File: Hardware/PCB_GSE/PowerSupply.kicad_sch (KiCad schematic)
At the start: 67 parts, among them J2 Vin_XT30PW-F, U2 MPQ9843GLE-5-AEC1-Z, U3 MP28167GQ-B-P, U4 TLV75733PDBVR

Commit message: fix : done silkscreen and finition
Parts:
- renumbered C44 to C21, C42 to C30, C32 to C31, C36 to C33, C24 to C34, C19 to C35, C43 to C36, C33 to C37, C16 to C38, C41 to C39, C22 to C40, C13 to C41, C34 to C42, C12 to C43, C26 to C44, C18 to C45, C21 to C46, C14 to C47, C29 to C48, C31 to C49, C15 to C50, C25 to C51, C23 to C52, C20 to C53, C17 to C54, C39 to C55, C38 to C56, C37 to C57, C35 to C58, C28 to C59, C40 to C60, C27 to C61, C30 to C62, LED4 to D6, LED2 to D7, LED3 to D8, FB2 to FB4, J2 to J8, L2 to L1, L1 to L2, R33 to R18, R31 to R20, R34 to R26, R35 to R27, R26 to R28, R30 to R31, R22 to R33, R17 to R34, R18 to R35, R29 to R36, R20 to R37, R15 to R38, R14 to R39, R27 to R40, R28 to R41, R19 to R42, R16 to R43, R21 to R44, R23 to R45, R25 to R46, R24 to R47, U3 to U10, U2 to U8, U4 to U9

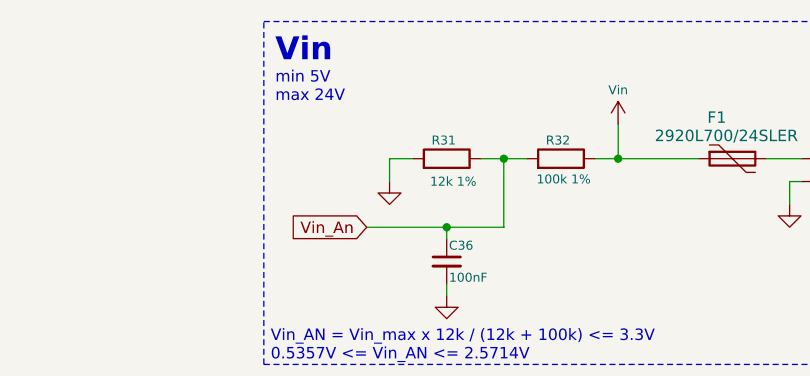
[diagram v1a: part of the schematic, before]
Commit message: fix(gse): Vin servo
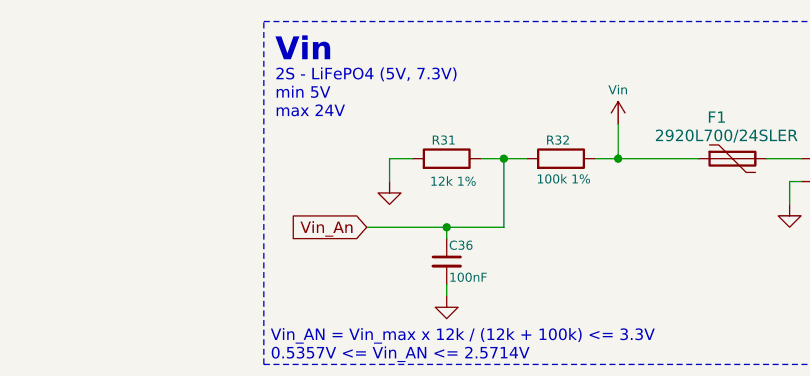
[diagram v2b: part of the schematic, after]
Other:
- note added: "2S - LiFePO4 (5V, 7.3V) min 5V max 24V"
- note removed: "min 5V max 24V"
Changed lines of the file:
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@@
 		)
 	)
-	(text "min 5V\nmax 24V"
+	(text "2S - LiFePO4 (5V, 7.3V)\nmin 5V\nmax 24V"
 		(exclude_from_sim no)
-		(at 208.28 18.288 0)
+		(at 208.28 18.034 0)
 		(effects
 			(font

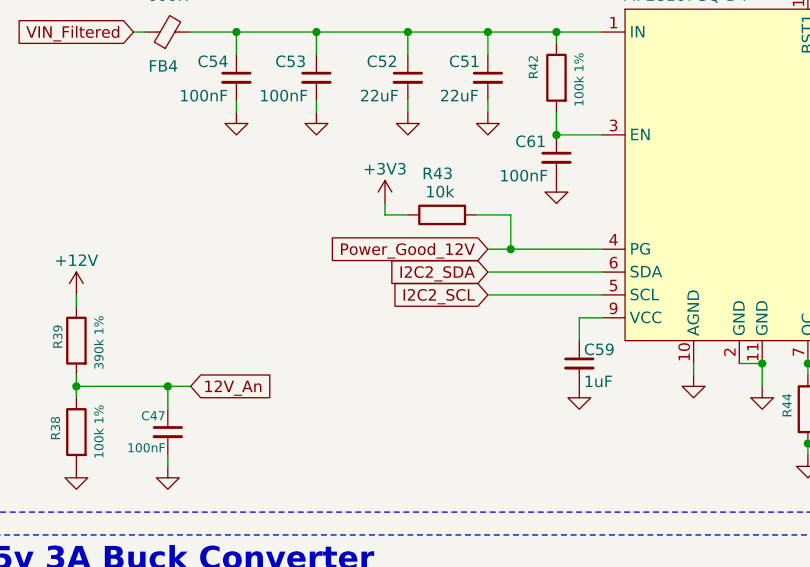
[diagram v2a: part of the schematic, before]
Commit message: fix(gse): change Servo3_PWM -> TIM1_CH2, change Valve1/2_Open pin
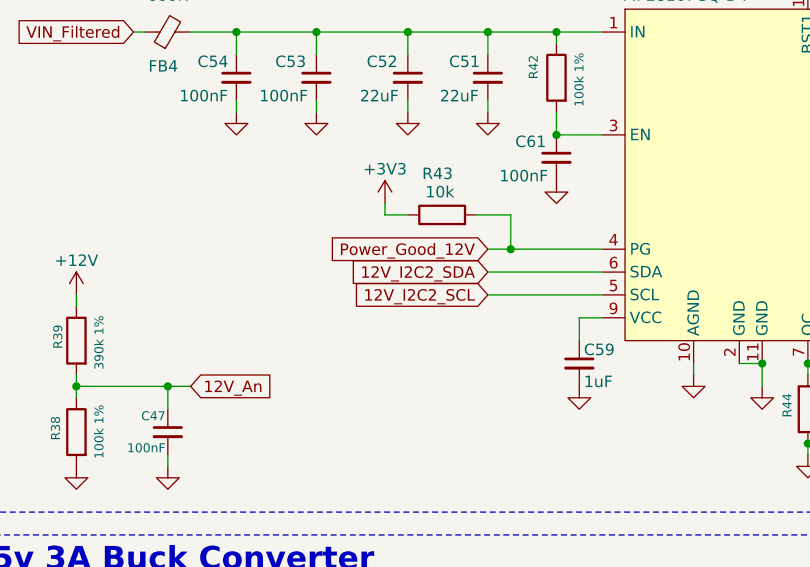
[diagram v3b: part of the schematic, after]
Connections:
- net I2C2_SCL renamed 12V_I2C2_SCL
- net I2C2_SDA renamed 12V_I2C2_SDA
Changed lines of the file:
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@@
 		)
 	)
-	(global_label "I2C2_SDA"
+	(global_label "12V_I2C2_SDA"
 		(shape input)
 		(at 69.85 96.52 180)
@@
 		)
 		(property "Intersheetrefs" "${INTERSHEET_REFS}"
-			(at 58.0353 96.52 0)
+			(at 53.5601 96.52 0)
 			(effects
 				(font
@@
 		)
 	)
-	(global_label "I2C2_SCL"
+	(global_label "12V_I2C2_SCL"
 		(shape input)
 		(at 69.85 99.06 180)
@@
 		)
 		(property "Intersheetrefs" "${INTERSHEET_REFS}"
-			(at 58.0958 99.06 0)
+			(at 53.6206 99.06 0)
 			(effects
 				(font

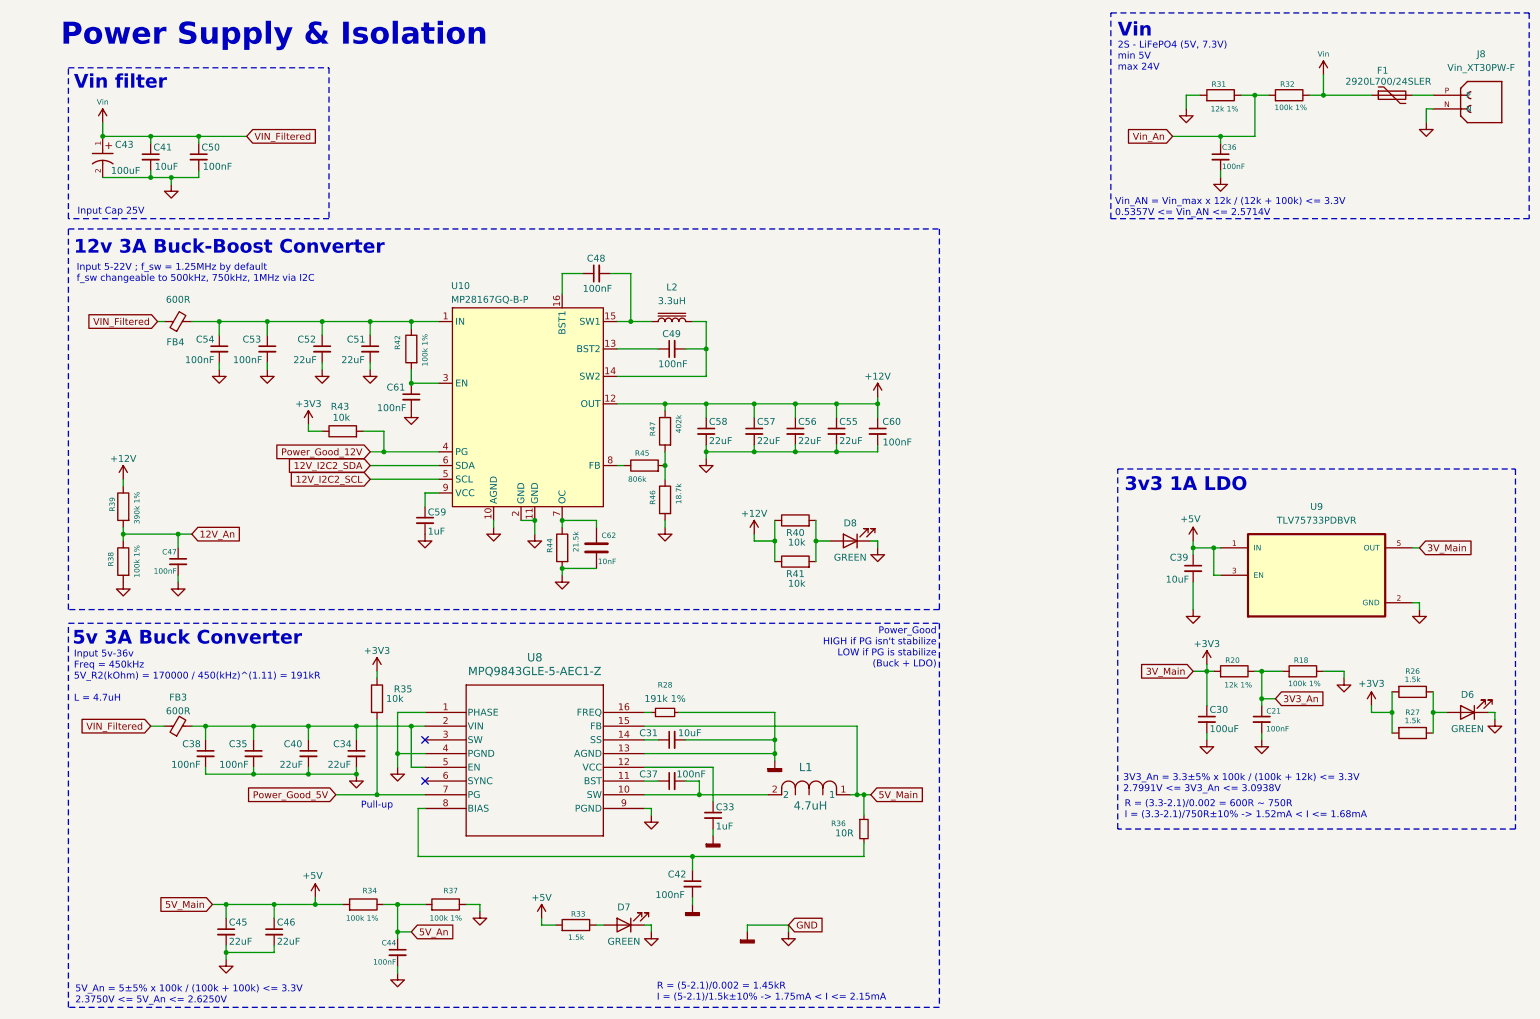
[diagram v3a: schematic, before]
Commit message: fix: silkscreen green<->black + fix silkscreen + connect shield to gnd  in pressure sensor + fix/add doc
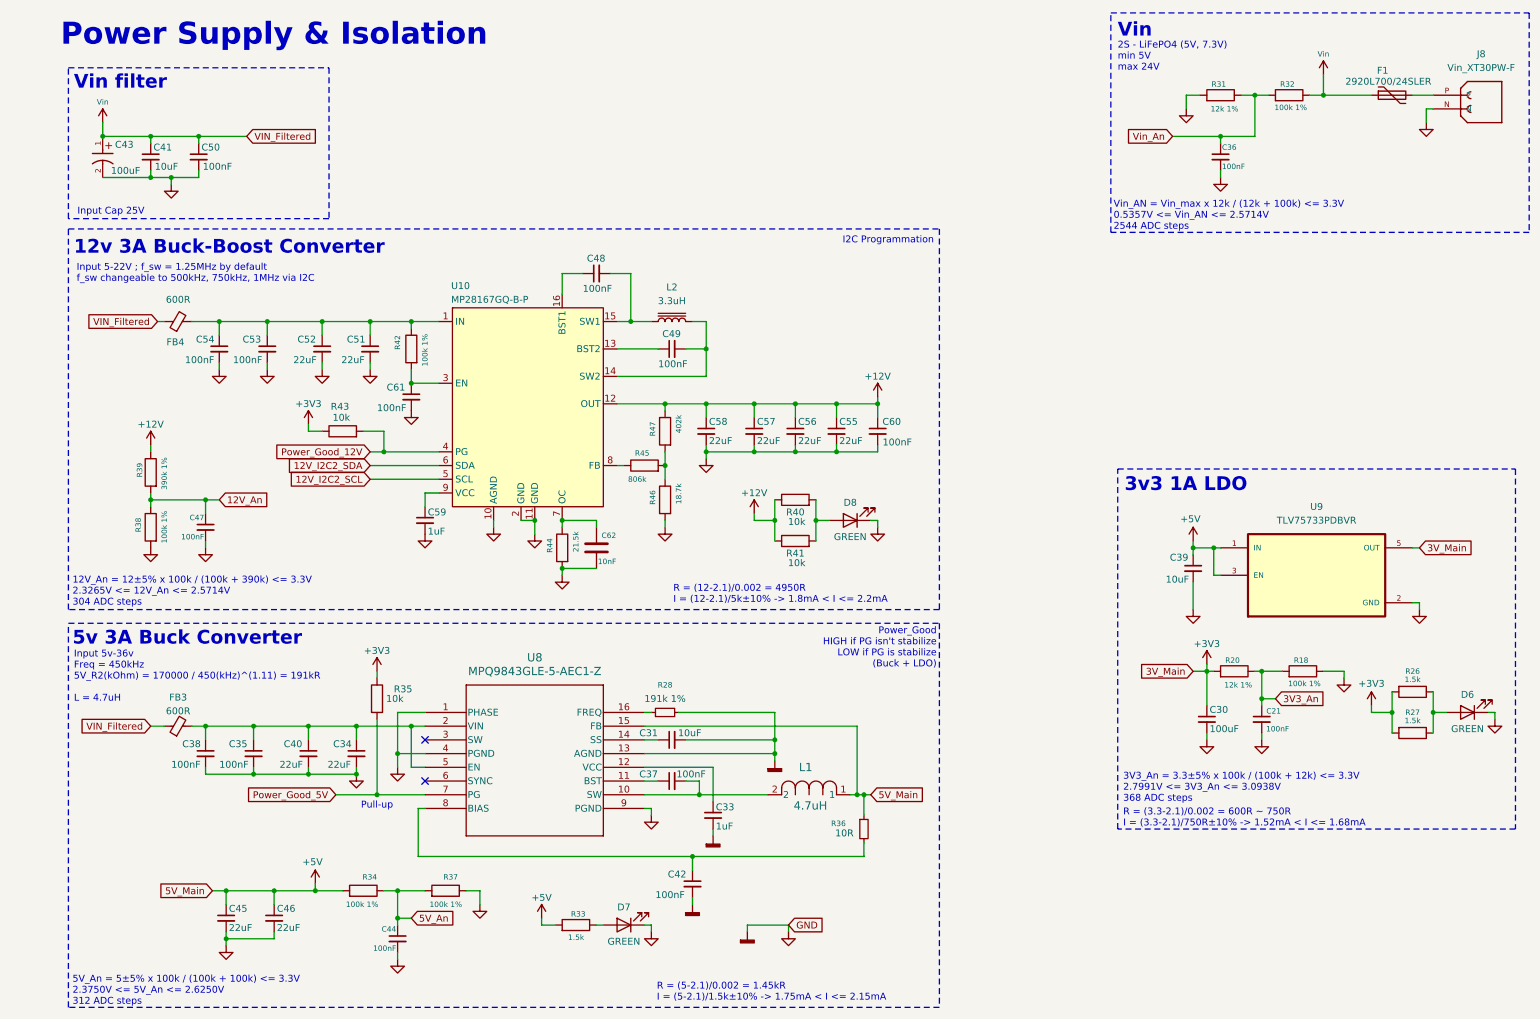
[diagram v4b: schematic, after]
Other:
- note added: "12V_An = 12±5% x 100k / (100k + 390k) <= 3.3V 2.3265V <= 12V_An <= 2.5714V 304 ADC steps"
- note added: "3V3_An = 3.3±5% x 100k / (100k + 12k) <= 3.3V 2.7991V <= 3V3_An <= 3.0938V 368 ADC steps"
- note added: "5V_An = 5±5% x 100k / (100k + 100k) <= 3.3V 2.3750V <= 5V_An <= 2.6250V 312 ADC steps"
- note added: "I2C Programmation"
- note added: "R = (12-2.1)/0.002 = 4950R I = (12-2.1)/5k±10% -> 1.8mA < I <= 2.2mA"
- note added: "Vin_AN = Vin_max x 12k / (12k + 100k) <= 3.3V 0.5357V <= Vin_AN <= 2.5714V 2544 ADC steps"
- note removed: "3V3_An = 3.3±5% x 100k / (100k + 12k) <= 3.3V 2.7991V <= 3V3_An <= 3.0938V"
- note removed: "5V_An = 5±5% x 100k / (100k + 100k) <= 3.3V 2.3750V <= 5V_An <= 2.6250V"
- note removed: "Vin_AN = Vin_max x 12k / (12k + 100k) <= 3.3V 0.5357V <= Vin_AN <= 2.5714V"
- moved on the sheet: C44, C45, C46, C47, D8, R34, R37, R38, R39, R40, R41

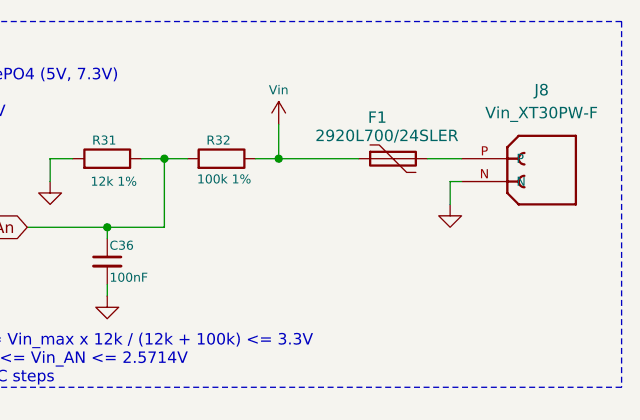
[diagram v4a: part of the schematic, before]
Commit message: fix : add polyfuses and fix 90 deg servo connectors
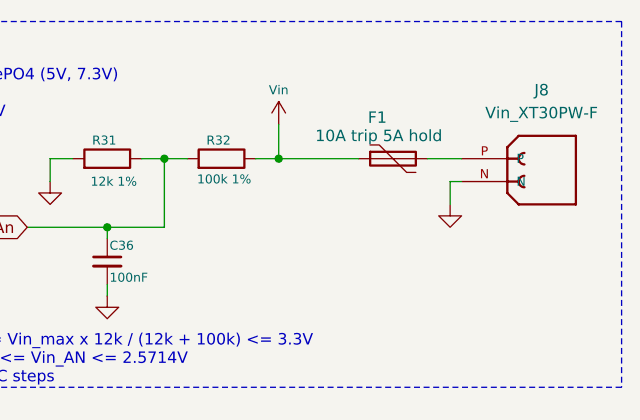
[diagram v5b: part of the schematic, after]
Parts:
- F1: value 2920L700/24SLER -> 10A trip 5A hold; DigiKey_Part_Number 18-2920L700/24SLERCT-ND -> 18-2920L500/24SLDRCT-ND; Manufacturer_Part_Number 2920L700/24SLER -> 2920L500/24SLDR
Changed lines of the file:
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@@
 			)
 		)
-		(property "Value" "2920L700/24SLER"
+		(property "Value" "10A trip 5A hold"
 			(at 250.444 25.4 90)
 			(effects
@@
 			)
 		)
-		(property "Datasheet" "https://www.digikey.ca/en/products/detail/littelfuse-inc/2920L700-24SLER/12807015"
+		(property "Datasheet" "https://www.digikey.ca/en/products/detail/littelfuse-inc/2920L500-24SLDR/12807024"
 			(at 259.08 27.94 0)
 			(effects
@@
 			)
 		)
-		(property "DigiKey_Part_Number" "18-2920L700/24SLERCT-ND"
+		(property "DigiKey_Part_Number" "18-2920L500/24SLDRCT-ND"
 			(at 259.08 27.94 90)
 			(effects
@@
 			)
 		)
-		(property "Manufacturer_Part_Number" "2920L700/24SLER"
+		(property "Manufacturer_Part_Number" "2920L500/24SLDR"
 			(at 259.08 27.94 90)
 			(effects

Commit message: feature : Done v1 and send to fab
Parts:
- C33, C59: DigiKey_Part_Number 399-C0603C105K4RACTUCT-ND -> 1276-1029-1-ND; Manufacturer_Part_Number C0603C105K4RACTU -> CL21B105KBFNNNE
- J8: Manufacturer_Part_Number (none) -> -
- R26, R27, R33: DigiKey_Part_Number P1.5KDBCT-ND -> 311-1.50KCRCT-ND; Manufacturer_Part_Number ERA-3AEB152V -> RC0805FR-071K5L
- R28: DigiKey_Part_Number P191KDBCT-ND -> 311-191KCRCT-ND; Manufacturer_Part_Number ERA-3AEB1913V -> RC0805FR-07191KL
- R35, R40, R41, R43: DigiKey_Part_Number 311-10.0KHRCT-ND -> 541-10.0KCCT-ND; Manufacturer_Part_Number RC0603FR-0710KL -> CRCW080510K0FKEA
- R36: DigiKey_Part_Number 541-10.0LCT-ND -> 311-10.0CRCT-ND; Manufacturer_Part_Number CRCW040210R0FKED -> RC0805FR-0710RL
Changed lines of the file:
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@@
 			)
 		)
-		(property "Datasheet" "https://www.digikey.ca/en/products/detail/panasonic-electronic-components/ERA-3AEB152V/1465858"
+		(property "Datasheet" "https://www.digikey.ca/en/products/detail/yageo/RC0805FR-071K5L/727496"
 			(at 107.95 181.61 0)
 			(effects
@@
 			)
 		)
-		(property "DigiKey_Part_Number" "P1.5KDBCT-ND"
+		(property "DigiKey_Part_Number" "311-1.50KCRCT-ND"
 			(at 107.95 181.61 90)
 			(effects
@@
 			)
 		)
-		(property "Manufacturer_Part_Number" "ERA-3AEB152V"
+		(property "Manufacturer_Part_Number" "RC0805FR-071K5L"
 			(at 107.95 181.61 90)
 			(effects
@@
 			)
 		)
-		(property "Datasheet" ""
+		(property "Datasheet" "-"
 			(at 271.78 27.94 0)
 			(effects
@@
 			)
 		)
+		(property "Manufacturer_Part_Number" "-"
+			(at 271.78 27.94 0)
+			(effects
+				(font
+					(size 1.27 1.27)
+				)
+				(hide yes)
+			)
+		)
 		(pin "N"
 		)
@@
 			)
 		)
-		(property "Datasheet" "https://www.digikey.ca/en/products/detail/panasonic-electronic-components/ERA-3AEB1913V/2026952"
+		(property "Datasheet" "https://www.digikey.ca/en/products/detail/yageo/RC0805FR-07191KL/727660"
 			(at 124.46 142.24 0)
 			(effects
@@
 			)
 		)
-		(property "DigiKey_Part_Number" "P191KDBCT-ND"
+		(property "DigiKey_Part_Number" "311-191KCRCT-ND"
 			(at 124.46 142.24 90)
 			(effects
@@
 			)
 		)
-		(property "Manufacturer_Part_Number" "ERA-3AEB1913V"
+		(property "Manufacturer_Part_Number" "RC0805FR-07191KL"
 			(at 124.46 142.24 90)
 			(effects
@@
 			)
 		)
-		(property "Datasheet" "https://www.digikey.ca/en/products/detail/panasonic-electronic-components/ERA-3AEB152V/1465858"
+		(property "Datasheet" "https://www.digikey.ca/en/products/detail/yageo/RC0805FR-071K5L/727496"
 			(at 262.89 138.43 0)
 			(effects
@@
 			)
 		)
-		(property "DigiKey_Part_Number" "P1.5KDBCT-ND"
+		(property "DigiKey_Part_Number" "311-1.50KCRCT-ND"
 			(at 262.89 138.43 90)
 			(effects
@@
 			)
 		)
-		(property "Manufacturer_Part_Number" "ERA-3AEB152V"
+		(property "Manufacturer_Part_Number" "RC0805FR-071K5L"
 			(at 262.89 138.43 90)
 			(effects
@@
 			)
 		)
-		(property "Datasheet" "https://www.digikey.ca/en/products/detail/panasonic-electronic-components/ERA-3AEB152V/1465858"
+		(property "Datasheet" "https://www.digikey.ca/en/products/detail/yageo/RC0805FR-071K5L/727496"
 			(at 262.89 146.05 0)
 			(effects
@@
 			)
 		)
-		(property "DigiKey_Part_Number" "P1.5KDBCT-ND"
+		(property "DigiKey_Part_Number" "311-1.50KCRCT-ND"
 			(at 262.89 146.05 90)
 			(effects
@@
 			)
 		)
-		(property "Manufacturer_Part_Number" "ERA-3AEB152V"
+		(property "Manufacturer_Part_Number" "RC0805FR-071K5L"
 			(at 262.89 146.05 90)
 			(effects
@@
 			)
 		)
-		(property "Datasheet" "https://www.digikey.ca/en/products/detail/yageo/RC0603FR-0710KL/726880"
+		(property "Datasheet" "https://www.digikey.ca/en/products/detail/vishay-dale/CRCW080510K0FKEA/1175751"
 			(at 71.12 139.7 0)
 			(effects
@@
 			)
 		)
-		(property "DigiKey_Part_Number" "311-10.0KHRCT-ND"
+		(property "DigiKey_Part_Number" "541-10.0KCCT-ND"
 			(at 71.12 139.7 0)
 			(effects
@@
 			)
 		)
-		(property "Manufacturer_Part_Number" "RC0603FR-0710KL"
+		(property "Manufacturer_Part_Number" "CRCW080510K0FKEA"
 			(at 71.12 139.7 0)
 			(effects
@@
 			)
 		)
-		(property "Datasheet" "https://www.digikey.ca/en/products/detail/yageo/RC0603FR-0710KL/726880"
+		(property "Datasheet" "https://www.digikey.ca/en/products/detail/vishay-dale/CRCW080510K0FKEA/1175751"
 			(at 148.59 110.49 0)
 			(effects
@@
 			)
 		)
-		(property "DigiKey_Part_Number" "311-10.0KHRCT-ND"
+		(property "DigiKey_Part_Number" "541-10.0KCCT-ND"
 			(at 148.59 110.49 0)
 			(effects
@@
 			)
 		)
-		(property "Manufacturer_Part_Number" "RC0603FR-0710KL"
+		(property "Manufacturer_Part_Number" "CRCW080510K0FKEA"
 			(at 148.59 110.49 0)
 			(effects
@@
 			)
 		)
-		(property "Datasheet" "https://www.digikey.ca/en/products/detail/yageo/RC0603FR-0710KL/726880"
+		(property "Datasheet" "https://www.digikey.ca/en/products/detail/vishay-dale/CRCW080510K0FKEA/1175751"
 			(at 64.77 90.17 0)
 			(effects
@@
 			)
 		)
-		(property "DigiKey_Part_Number" "311-10.0KHRCT-ND"
+		(property "DigiKey_Part_Number" "541-10.0KCCT-ND"
 			(at 64.77 90.17 0)
 			(effects
@@
 			)
 		)
-		(property "Manufacturer_Part_Number" "RC0603FR-0710KL"
+		(property "Manufacturer_Part_Number" "CRCW080510K0FKEA"
 			(at 64.77 90.17 0)
 			(effects
@@
 			)
 		)
-		(property "Datasheet" "https://www.digikey.ca/en/products/detail/yageo/RC0603FR-0710KL/726880"
+		(property "Datasheet" "https://www.digikey.ca/en/products/detail/vishay-dale/CRCW080510K0FKEA/1175751"
 			(at 148.59 102.87 0)
 			(effects
@@
 			)
 		)
-		(property "DigiKey_Part_Number" "311-10.0KHRCT-ND"
+		(property "DigiKey_Part_Number" "541-10.0KCCT-ND"
 			(at 148.59 102.87 0)
 			(effects
@@
 			)
 		)
-		(property "Manufacturer_Part_Number" "RC0603FR-0710KL"
+		(property "Manufacturer_Part_Number" "CRCW080510K0FKEA"
 			(at 148.59 102.87 0)
 			(effects
@@
 			)
 		)
-		(property "Datasheet" "https://www.digikey.ca/en/products/detail/vishay-dale/CRCW040210R0FKED/1177779"
+		(property "Datasheet" "https://www.digikey.ca/en/products/detail/yageo/RC0805FR-0710RL/727534"
 			(at 161.29 163.83 0)
 			(effects
@@
 			)
 		)
-		(property "DigiKey_Part_Number" "541-10.0LCT-ND"
+		(property "DigiKey_Part_Number" "311-10.0CRCT-ND"
 			(at 161.29 163.83 0)
 			(effects
@@
 			)
 		)
-		(property "Manufacturer_Part_Number" "CRCW040210R0FKED"
+		(property "Manufacturer_Part_Number" "RC0805FR-0710RL"
 			(at 161.29 163.83 0)
 			(effects
@@
 			)
 		)
-		(property "Datasheet" "https://www.digikey.ca/en/products/detail/kemet/C0603C105K4RACTU/2199788"
+		(property "Datasheet" "https://www.digikey.ca/en/products/detail/samsung-electro-mechanics/CL21B105KBFNNNE/3886687"
 			(at 80.01 106.68 0)
 			(effects
@@
 			)
 		)
-		(property "DigiKey_Part_Number" "399-C0603C105K4RACTUCT-ND"
+		(property "DigiKey_Part_Number" "1276-1029-1-ND"
 			(at 80.01 106.68 0)
 			(effects
@@
 			)
 		)
-		(property "Manufacturer_Part_Number" "C0603C105K4RACTU"
+		(property "Manufacturer_Part_Number" "CL21B105KBFNNNE"
 			(at 80.01 106.68 0)
 			(effects
@@
 			)
 		)
-		(property "Datasheet" "https://www.digikey.ca/en/products/detail/kemet/C0603C105K4RACTU/2199788"
+		(property "Datasheet" "https://www.digikey.ca/en/products/detail/samsung-electro-mechanics/CL21B105KBFNNNE/3886687"
 			(at 133.35 161.29 0)
 			(effects
@@
 			)
 		)
-		(property "DigiKey_Part_Number" "399-C0603C105K4RACTUCT-ND"
+		(property "DigiKey_Part_Number" "1276-1029-1-ND"
 			(at 133.35 161.29 0)
 			(effects
@@
 			)
 		)
-		(property "Manufacturer_Part_Number" "C0603C105K4RACTU"
+		(property "Manufacturer_Part_Number" "CL21B105KBFNNNE"
 			(at 133.35 161.29 0)
 			(effects
